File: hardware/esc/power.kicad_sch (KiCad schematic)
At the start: 43 parts, among them U1 TPS563200, U2 NCP59800BMNADJTAG

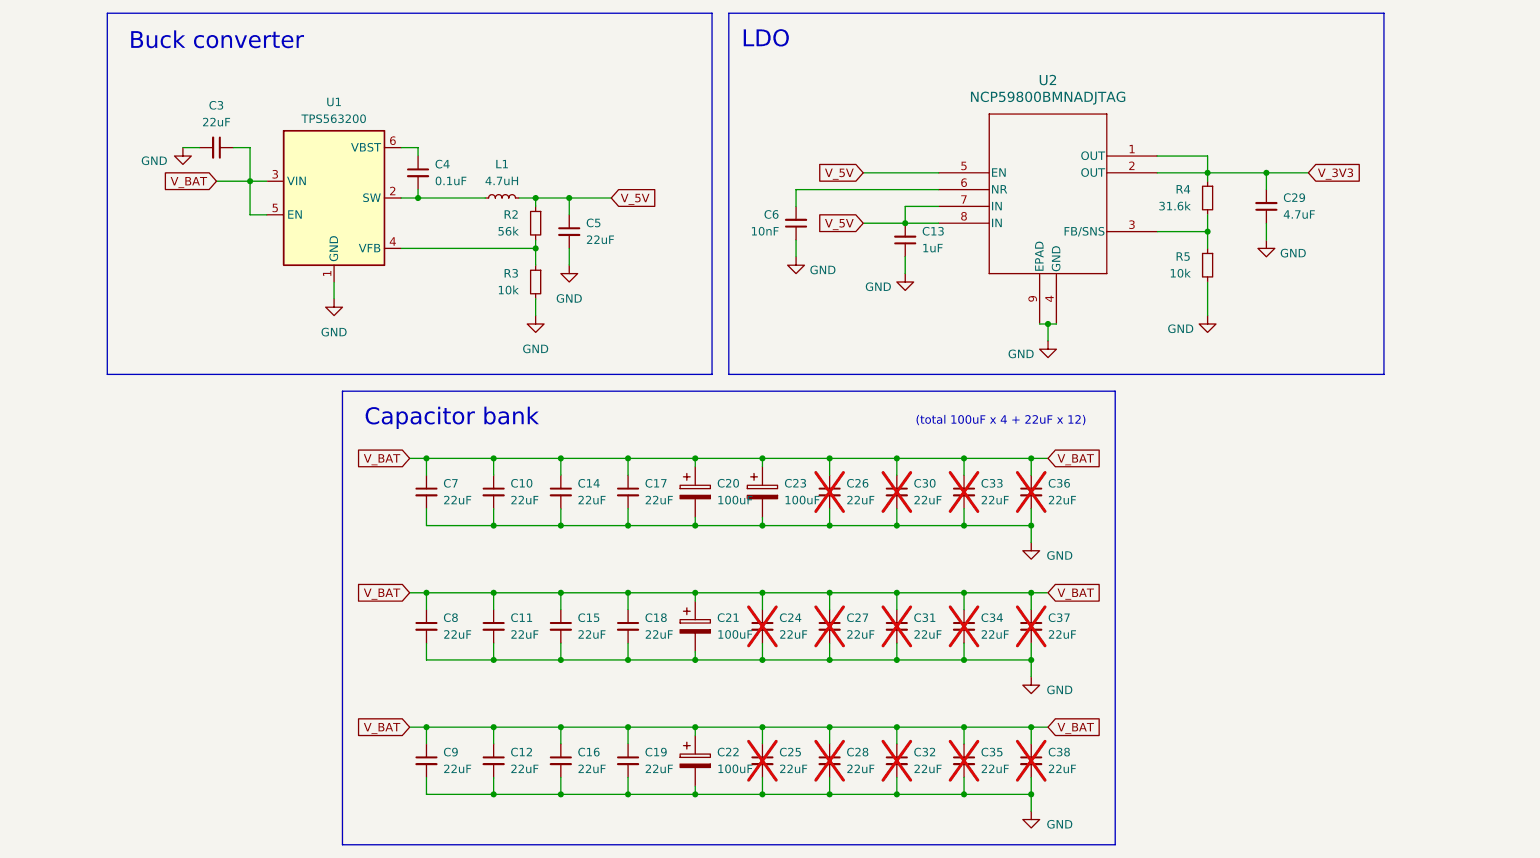
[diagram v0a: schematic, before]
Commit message: h/feat: preliminary rev 2 schematic
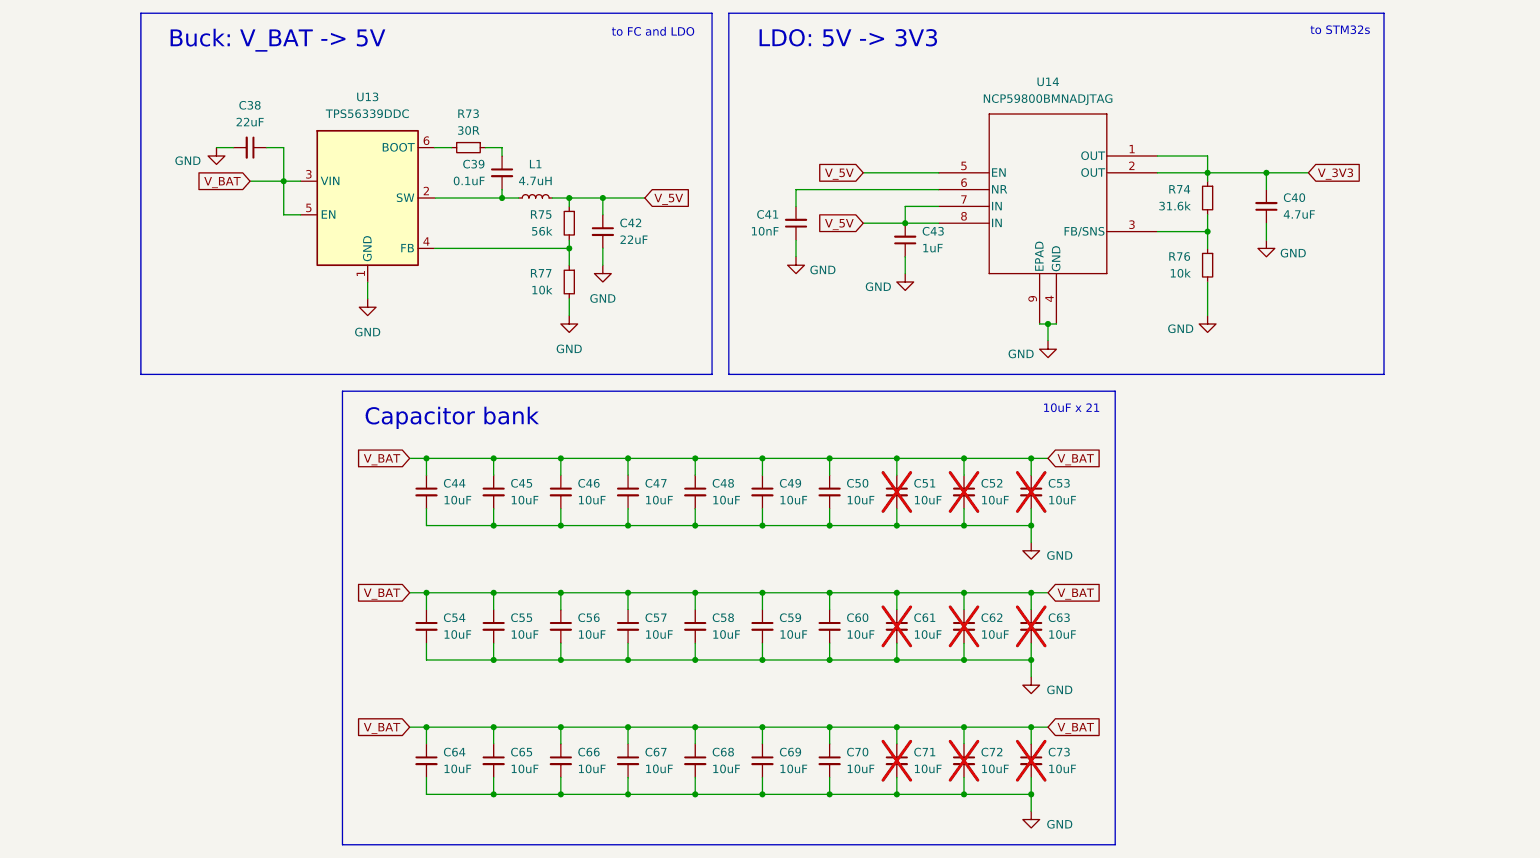
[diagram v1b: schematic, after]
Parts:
- removed C10, C11, C12, C14, C15, C16, C17, C18, C19, C24, C25, C26, C27, C28, C7, C8, C9: 22uF, Capacitor_SMD:C_0805_2012Metric, symbol Device:C_Small
- removed C20, C21, C22, C23: 100uF, Stratus:ECASD61C107M012KA0, symbol Device:C_Polarized
- removed U1: TPS563200, Stratus:TPS563200, symbol Regulator_Switching:TPS563200
- added C44, C45, C46, C47, C48, C49, C50, C54, C55, C56, C57, C58, C59, C60, C64, C65, C66, C67, C68, C69, C70: 10uF, Capacitor_SMD:C_0805_2012Metric, symbol Device:C_Small
- added R73: 30R, Resistor_SMD:R_0402_1005Metric, symbol Device:R_Small
- added U13: TPS56339DDC, Package_TO_SOT_SMD:SOT-23-6, symbol Regulator_Switching:TPS56339DDC
- C40: renamed from C29; footprint Capacitor_SMD:C_0603_1608Metric -> Capacitor_SMD:C_0402_1005Metric
- C51: renamed from C30; value 22uF -> 10uF
- C52: renamed from C33; value 22uF -> 10uF
- C53: renamed from C36; value 22uF -> 10uF
- C61: renamed from C31; value 22uF -> 10uF
- C62: renamed from C34; value 22uF -> 10uF
- C63: renamed from C37; value 22uF -> 10uF
- C71: renamed from C32; value 22uF -> 10uF
- C72: renamed from C35; value 22uF -> 10uF
- C73: renamed from C38; value 22uF -> 10uF
- renumbered C3 to C38, C4 to C39, C6 to C41, C5 to C42, C13 to C43, R4 to R74, R2 to R75, R5 to R76, R3 to R77, U2 to U14
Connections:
- net GND: now also C44.2, C45.2, C46.2, C47.2, C48.2, C49.2, C50.2, C54.2, C55.2, C56.2, C57.2, C58.2, C59.2, C60.2, C64.2, C65.2, C66.2, C67.2, C68.2, C69.2, C70.2, U13.1 (GND)
- net V_BAT: now also C44.1, C45.1, C46.1, C47.1, C48.1, C49.1, C50.1, C54.1, C55.1, C56.1, C57.1, C58.1, C59.1, C60.1, C64.1, C65.1, C66.1, C67.1, C68.1, C69.1, C70.1, U13.3 (VIN), U13.5 (EN)
- net at C39.1: now also R73.1
- net at C39.2, L1.1: now also U13.2 (SW)
- net at R75.2, R77.1: now also U13.4 (FB)
- new net: R73.2, U13.6 (BOOT)
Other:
- note added: "10uF x 21"
- note added: "Buck: V_BAT -> 5V"
- note added: "LDO: 5V -> 3V3"
- note added: "to FC and LDO"
- note added: "to STM32s"
- note removed: "(total 100uF x 4 + 22uF x 12)"
- note removed: "Buck converter"
- note removed: "LDO"
- moved on the sheet: C38, C39, C42, L1, R75, R77

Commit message: chore: prep: footprints, 3d models, pcb
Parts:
- U13: footprint Package_TO_SOT_SMD:SOT-23-6 -> Stratus:TPS56339DDC
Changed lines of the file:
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@@
 			)
 		)
-		(property "Footprint" "Package_TO_SOT_SMD:SOT-23-6"
+		(property "Footprint" "Stratus:TPS56339DDC"
 			(at 95.25 57.15 0)
 			(hide yes)

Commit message: h/feat: gate drive routing + prelim layout
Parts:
- C39, C40, C41, C43: footprint Capacitor_SMD:C_0402_1005Metric -> Stratus:C_0402
- R73, R74, R75, R76, R77: footprint Resistor_SMD:R_0402_1005Metric -> Stratus:R_0402
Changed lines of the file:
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@@
 			)
 		)
-		(property "Footprint" "Resistor_SMD:R_0402_1005Metric"
+		(property "Footprint" "Stratus:R_0402"
 			(at 109.22 48.26 0)
 			(hide yes)
@@
 			)
 		)
-		(property "Footprint" "Capacitor_SMD:C_0402_1005Metric"
+		(property "Footprint" "Stratus:C_0402"
 			(at 114.3 52.07 0)
 			(hide yes)
@@
 			)
 		)
-		(property "Footprint" "Resistor_SMD:R_0402_1005Metric"
+		(property "Footprint" "Stratus:R_0402"
 			(at 220.98 55.88 0)
 			(hide yes)
@@
 			)
 		)
-		(property "Footprint" "Capacitor_SMD:C_0402_1005Metric"
+		(property "Footprint" "Stratus:C_0402"
 			(at 158.75 59.69 0)
 			(hide yes)
@@
 			)
 		)
-		(property "Footprint" "Resistor_SMD:R_0402_1005Metric"
+		(property "Footprint" "Stratus:R_0402"
 			(at 220.98 66.04 0)
 			(hide yes)
@@
 			)
 		)
-		(property "Footprint" "Resistor_SMD:R_0402_1005Metric"
+		(property "Footprint" "Stratus:R_0402"
 			(at 124.46 68.58 0)
 			(hide yes)
@@
 			)
 		)
-		(property "Footprint" "Resistor_SMD:R_0402_1005Metric"
+		(property "Footprint" "Stratus:R_0402"
 			(at 124.46 59.69 0)
 			(hide yes)
@@
 			)
 		)
-		(property "Footprint" "Capacitor_SMD:C_0402_1005Metric"
+		(property "Footprint" "Stratus:C_0402"
 			(at 175.26 62.23 0)
 			(hide yes)
@@
 			)
 		)
-		(property "Footprint" "Capacitor_SMD:C_0402_1005Metric"
+		(property "Footprint" "Stratus:C_0402"
 			(at 229.87 57.15 0)
 			(hide yes)

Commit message: h/feat: layout - 1/4 motors
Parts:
- removed C59, C60, C64, C65, C66, C67, C68, C69, C70, C73: 10uF, Capacitor_SMD:C_0805_2012Metric, symbol Device:C_Small
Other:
- note added: "10uF * 12"
- note removed: "10uF x 21"

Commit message: h/feat: layout
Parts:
- C61, C62: now fitted; now in the parts list
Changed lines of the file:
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@@
 		(body_style 1)
 		(exclude_from_sim no)
-		(in_bom no)
-		(on_board no)
+		(in_bom yes)
+		(on_board yes)
 		(in_pos_files yes)
-		(dnp yes)
+		(dnp no)
 		(fields_autoplaced yes)
 		(property "Reference" "C62"
@@
 		(body_style 1)
 		(exclude_from_sim no)
-		(in_bom no)
-		(on_board no)
+		(in_bom yes)
+		(on_board yes)
 		(in_pos_files yes)
-		(dnp yes)
+		(dnp no)
 		(fields_autoplaced yes)
 		(property "Reference" "C61"

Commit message: h/feat: power stage placement
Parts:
- added C65: 22uF, Capacitor_SMD:C_0805_2012Metric, symbol Device:C_Small
- C40: value 4.7uF -> 22uF; footprint Stratus:C_0402 -> Capacitor_SMD:C_0603_1608Metric
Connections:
- net GND: now also C65.2
- net V_5V: now also C65.1
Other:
- moved on the sheet: C40, C41, C43, R74, R76, U14

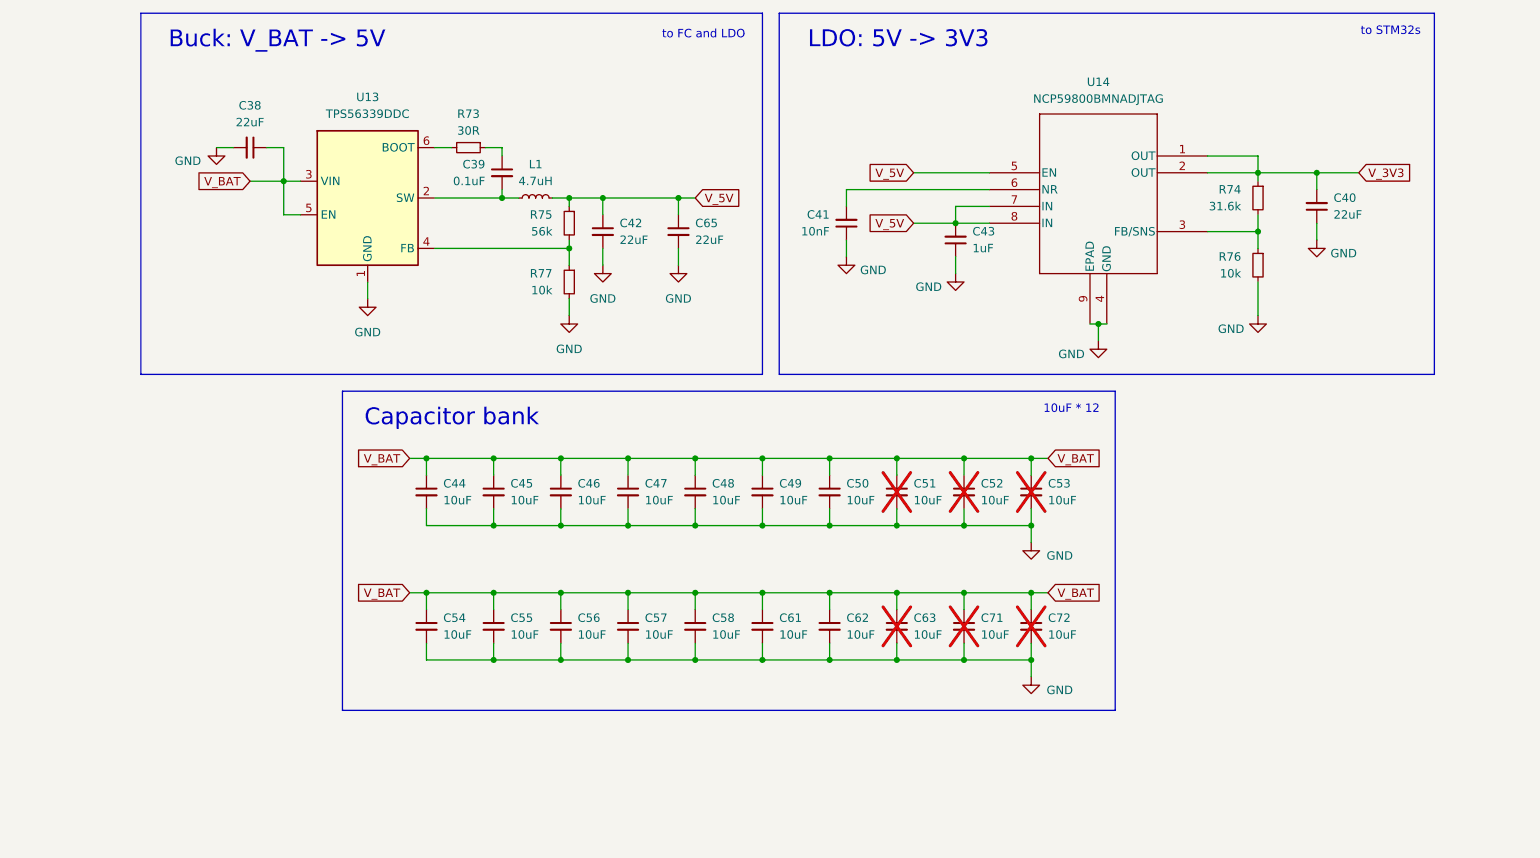
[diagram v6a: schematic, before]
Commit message: h/feat: power stage; finalise placement
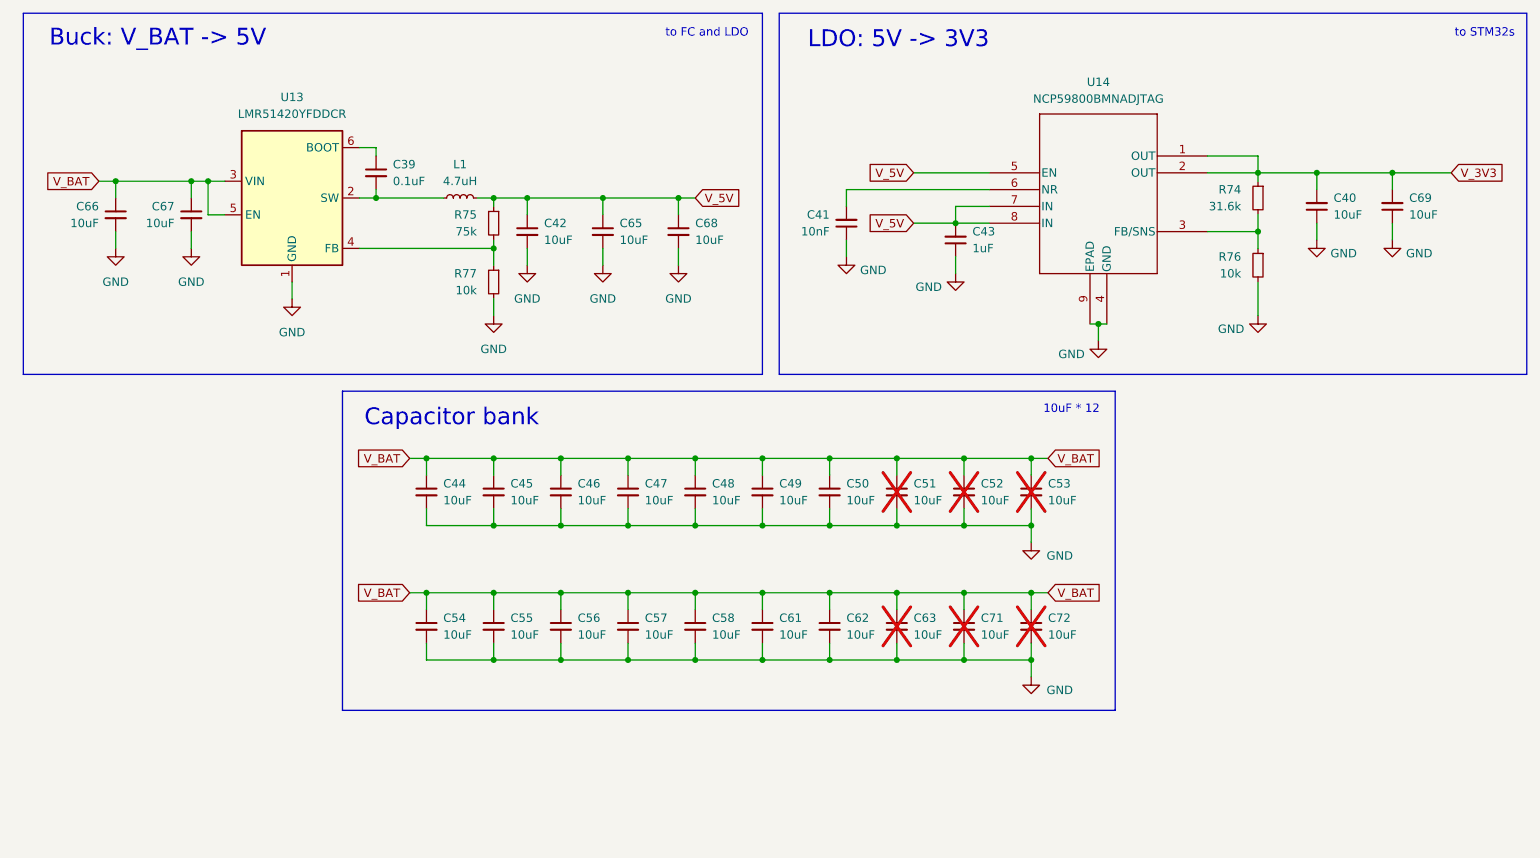
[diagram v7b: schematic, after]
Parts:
- removed C38: 22uF, Capacitor_SMD:C_0805_2012Metric, symbol Device:C_Small
- removed R73: 30R, Stratus:R_0402, symbol Device:R_Small
- added C66, C67: 10uF, Capacitor_SMD:C_0603_1608Metric, symbol Device:C_Small
- added C68, C69: 10uF, Stratus:C_0402, symbol Device:C_Small
- C40: value 22uF -> 10uF; footprint Capacitor_SMD:C_0603_1608Metric -> Stratus:C_0402
- C42, C65: value 22uF -> 10uF; footprint Capacitor_SMD:C_0805_2012Metric -> Stratus:C_0402
- L1: footprint Inductor_SMD:L_Taiyo-Yuden_MD-4040 -> Inductor_SMD:L_1210_3225Metric
- R75: value 56k -> 75k
- U13: value TPS56339DDC -> LMR51420YFDDCR; footprint Stratus:TPS56339DDC -> Stratus:LMR51420YFDDCR
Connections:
- net GND: now also C66.2, C67.2, C68.2, C69.1
- net V_3V3: now also C69.2
- net V_5V: now also C68.1
- net V_BAT: now also C66.1, C67.1
- net at C39.1: now also U13.6 (BOOT)
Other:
- moved on the sheet: C39, C42, C65, L1, R75, R77, U13

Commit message: h/feat: rework power stage: power drv8300 from 10v; remove 5v FC passthrough
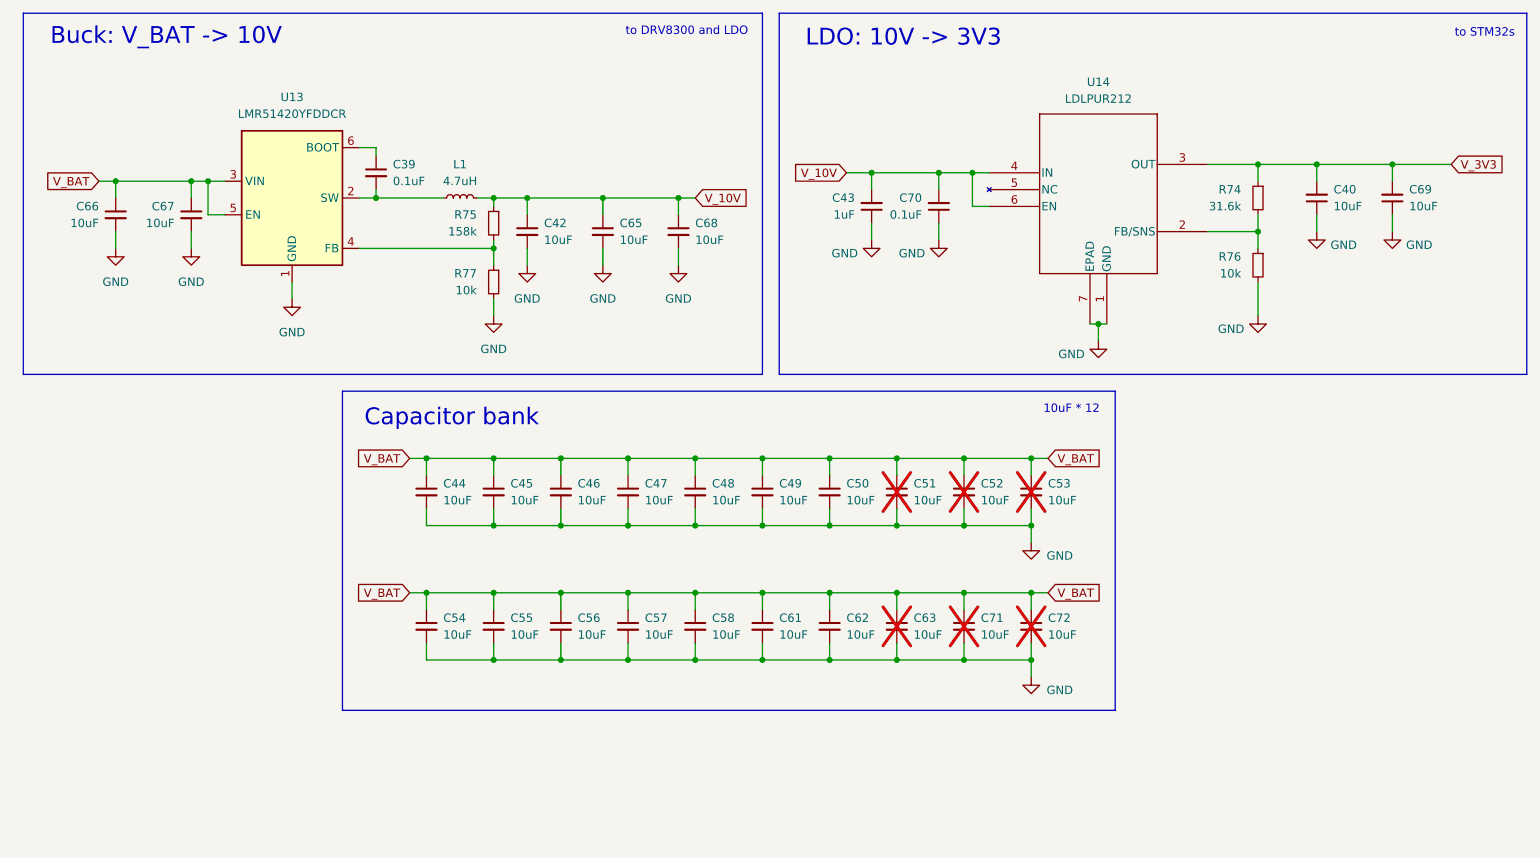
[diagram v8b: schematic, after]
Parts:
- removed C41: 10nF, Stratus:C_0402, symbol Device:C_Small
- added C70: 0.1uF, Stratus:C_0402, symbol Device:C_Small
- R75: value 75k -> 158k
- U14: value NCP59800BMNADJTAG -> LDLPUR212; footprint Stratus:NCP59800BMNADJTAG -> Stratus:LDLPUR212
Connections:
- net GND: now also U14.1 (GND), U14.7 (EPAD), C70.1; no longer U14.4 (GND), U14.9 (EPAD)
- net V_3V3: now also U14.3 (OUT); no longer U14.1 (OUT), U14.2 (OUT)
- net at R74.2, R76.1: now also U14.2 (FB/SNS); no longer U14.3 (FB/SNS)
- net V_10V: now reaches U14.6 (EN)
- net V_10V: now also C42.1, C43.2, C65.1, C68.1, L1.2, R75.1, U14.4 (IN), C70.2
- removed net V_5V: C42.1, C43.2, C65.1, C68.1, L1.2, R75.1, U14.5 (EN), U14.7 (IN), U14.8 (IN)
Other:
- note added: "Buck: V_BAT -> 10V"
- note added: "LDO: 10V -> 3V3"
- note added: "to DRV8300 and LDO"
- note removed: "Buck: V_BAT -> 5V"
- note removed: "LDO: 5V -> 3V3"
- note removed: "to FC and LDO"
- moved on the sheet: C40, C43, C69
